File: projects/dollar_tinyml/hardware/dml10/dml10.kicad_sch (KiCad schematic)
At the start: 52 parts, among them J1 Conn_01x03, J2 USB_A, J4 Header 2.54mm, J6 Conn_01x03, U1 PY32F003F16P6TU, U2 LTC4054, U3 BM7161, U5 LIS3DH, U6 LMV358

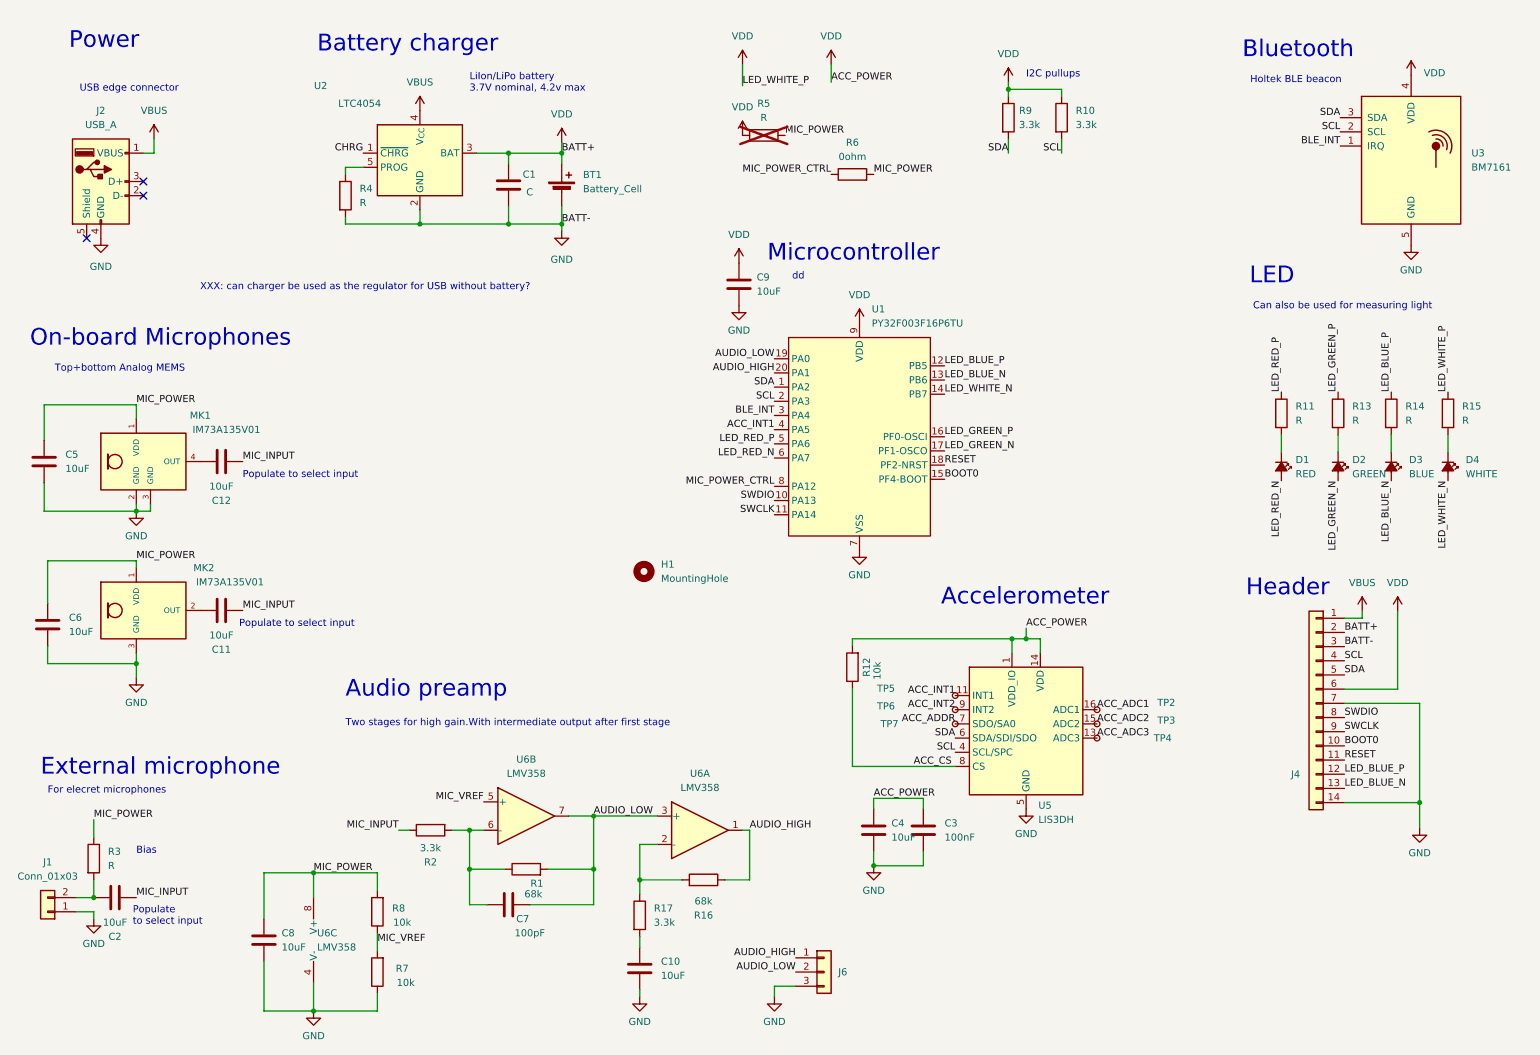
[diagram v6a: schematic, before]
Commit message: dollarml: Fixup BOM, submit to JLCPCB
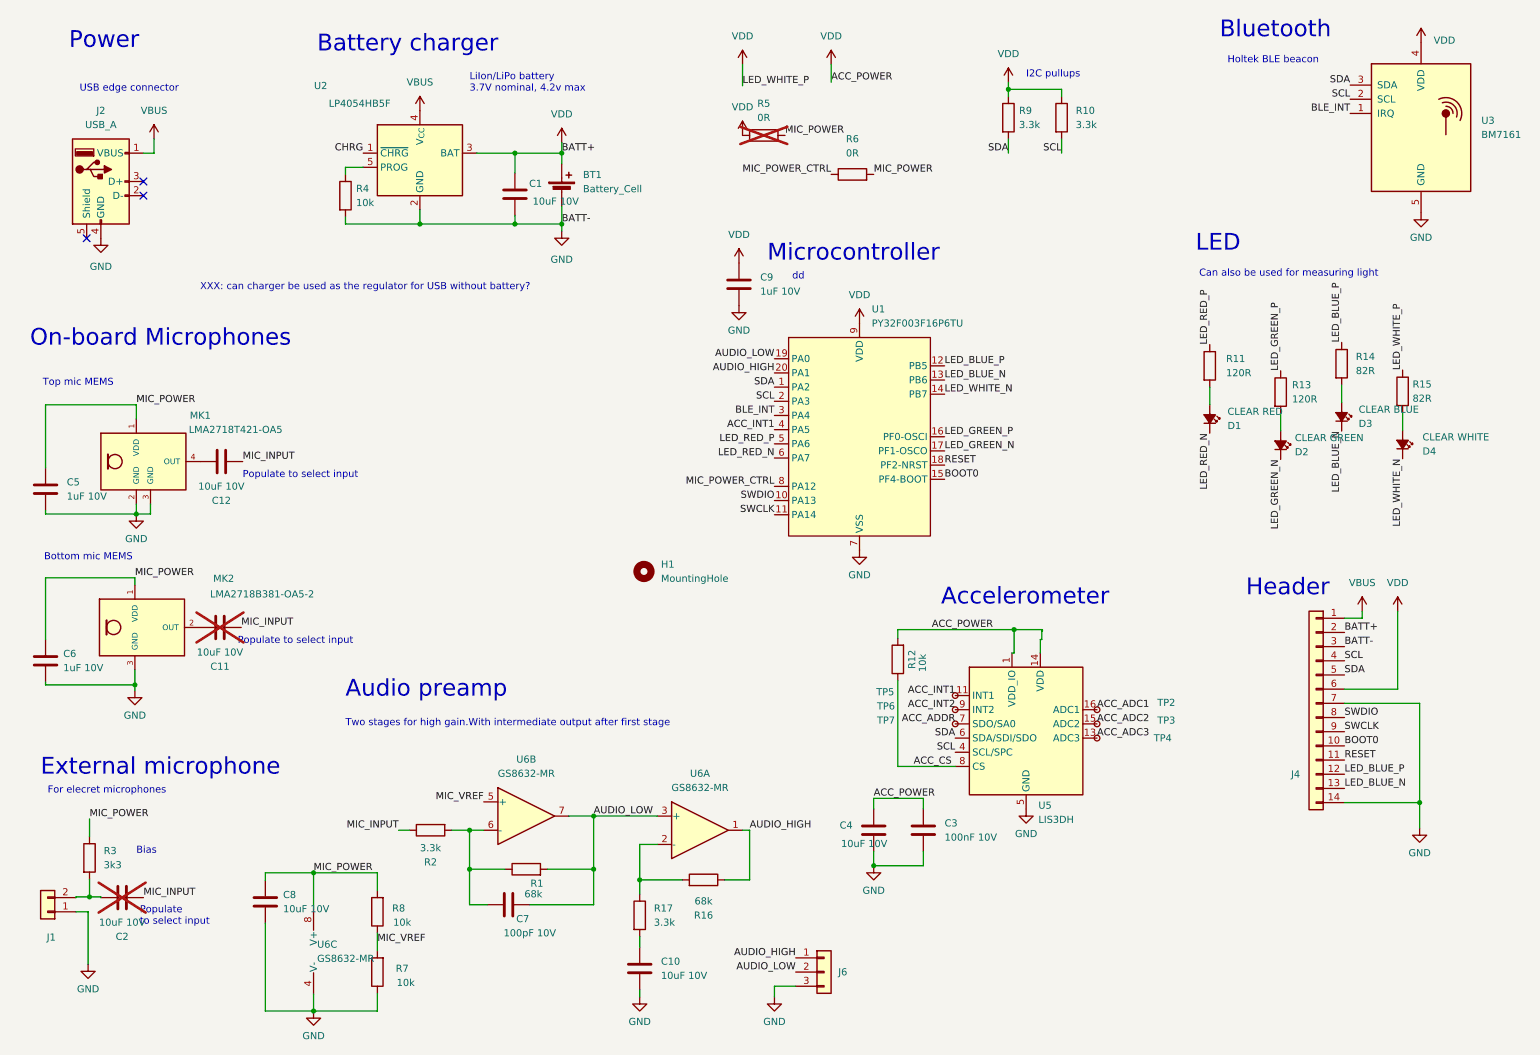
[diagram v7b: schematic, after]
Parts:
- BT1, H1, J2, J4, J6, TP2, TP3, TP4, TP5, TP6, TP7, U3: now left out of the parts list
- C1: value C -> 10uF 10V
- C10, C12, C4, C8: value 10uF -> 10uF 10V
- C11, C2: value 10uF -> 10uF 10V; now not fitted
- C3: value 100nF -> 100nF 10V
- C5, C6, C9: value 10uF -> 1uF 10V
- C7: value 100pF -> 100pF 10V
- D1: value RED -> CLEAR RED
- D2: value GREEN -> CLEAR GREEN
- D3: value BLUE -> CLEAR BLUE
- D4: value WHITE -> CLEAR WHITE
- J1: value Conn_01x03 -> Header 2.54mm; now left out of the parts list
- MK1: value IM73A135V01 -> LMA2718T421-OA5; LCSC (none) -> C5373232
- MK2: value IM73A135V01 -> LMA2718B381-OA5-2; LCSC (none) -> C7587902; STANDARD Manufacturer Recommendations -> (none)
- R11, R13: value R -> 120R
- R14, R15: value R -> 82R
- R3: value R -> 3k3
- R4: value R -> 10k
- R5: value R -> 0R
- R6: value 0ohm -> 0R
- U1: LCSC (none) -> C3018713
- U2: value LTC4054 -> LP4054HB5F; LCSC (none) -> C517187
- U5: LCSC (none) -> C15134
- U6: value LMV358 -> GS8632-MR; LCSC (none) -> C157704
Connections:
- net LED_BLUE_N: now also D3.1 (K); no longer D3.2 (A)
- net LED_GREEN_N: now also D2.1 (K); no longer D2.2 (A)
- net LED_RED_N: now also D1.1 (K); no longer D1.2 (A)
- net LED_WHITE_N: now also D4.1 (K); no longer D4.2 (A)
- net at R13.2: now also D2.2 (A); no longer D2.1 (K)
- net at R15.2: now also D4.2 (A); no longer D4.1 (K)
- net at R14.2: now also D3.2 (A); no longer D3.1 (K)
- net at R11.2: now also D1.2 (A); no longer D1.1 (K)
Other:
- note added: "Bottom mic MEMS"
- note added: "Top mic MEMS"
- note removed: "Top+bottom Analog MEMS"
- moved on the sheet: C1, C5, C6, C8, D1, D2, D3, D4, MK2, R11, R12, R13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
